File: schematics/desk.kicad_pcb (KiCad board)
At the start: 2 copper layers, 87 x 123 mm, 34 parts, among them K1 energized = UP (raises desk), K2 energized = DOWN (lowers desk), Q1 IRLZ44N, Q2 2N7000, Q3 2N7000, Q4 BC337, Q5 BC327, U1 LM2596HV 29V-5V, U2 ESP32_DevKitC, U3 74HC123 250ms, U5 ACS724xLCTR-05AB, U6 74HC08

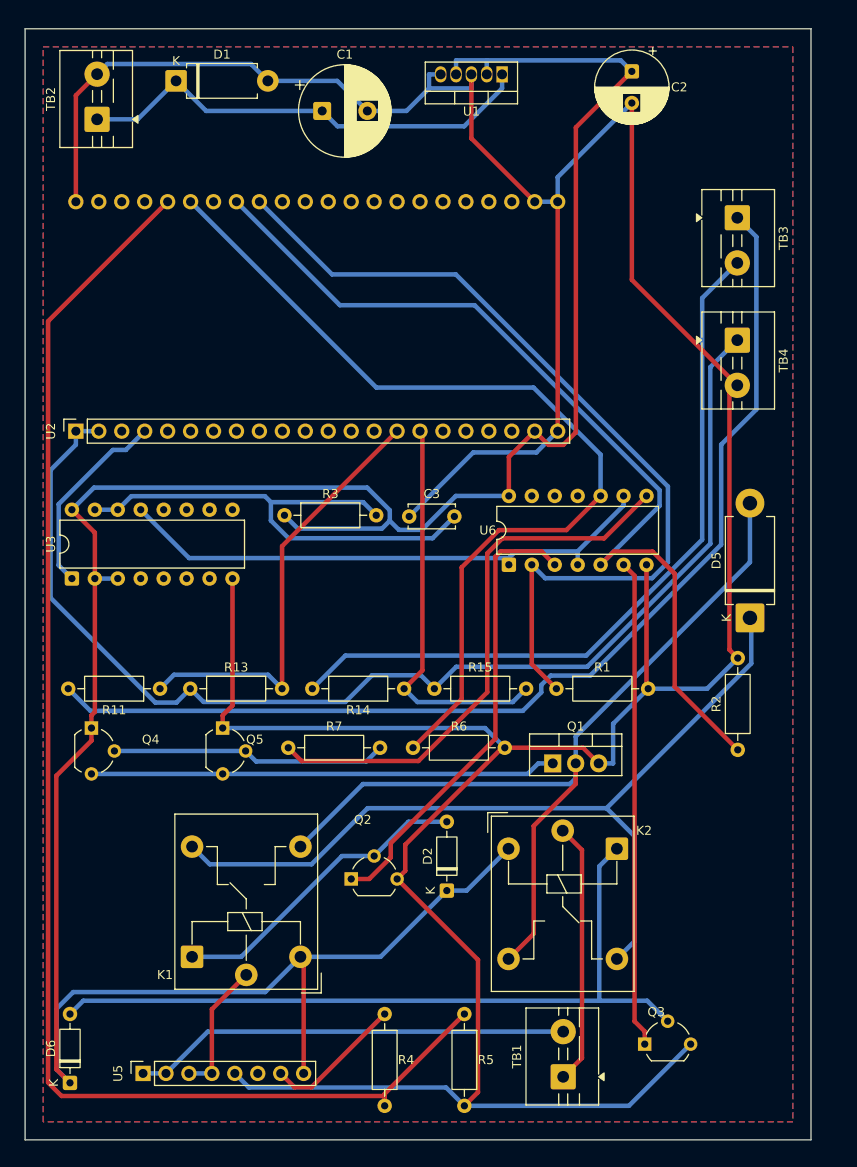
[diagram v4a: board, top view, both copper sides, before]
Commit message: Rotate R3/C3, shift U6/D5/R2/TB3/TB4 left: 87x123mm -> 85.5x123mm
R3 (12.3mm wide unrotated) and C3 (7.15mm wide unrotated) both have
much shorter dimensions on their other axis (6.44mm and 6.7mm) - both
fit easily within this row's height (driven by U6 at 18mm). Rotating
them 90 degrees freed 6.32mm of width in this row, which let U6, D5,
and R2 all shift left by that same amount.

R2 (now closer to R1 in the rocker row) needed a slightly smaller
shift than U6/D5 to keep 1.5mm clearance from R1 - not a uniform
block move, adjusted per-component to the nearest real constraint.

Once D5 stopped being the tightest thing in its row, TB3/TB4 (stacked
at the board's right edge) became the new binding width constraint
again - shifted them left too, down to what K2 (the actual widest
remaining item at 83.23mm) requires, rather than leaving them at the
old edge position out of inertia.

True footprint extent: 83.23 x 121.13mm (was 84.8 x 121.1mm - width
improved, height essentially unchanged since this pass didn't touch
row heights). Board outline: 85.5x123mm (was 87x123mm).

Re-routed from scratch, refilled both zones with the same settings as
recent commits. 0 vias, 0 unconnected, same accepted DRC profile
(isolated-copper + starved-thermal from the deliberate mill-fill
decision).
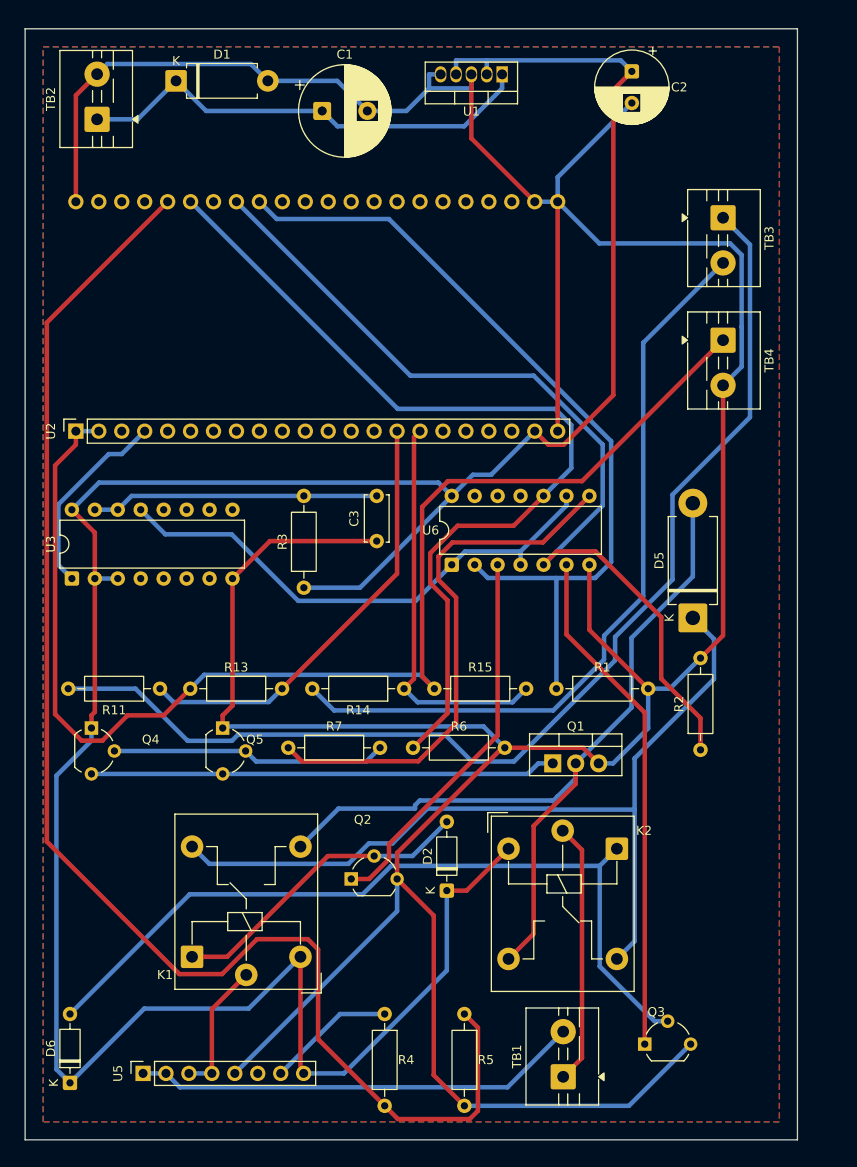
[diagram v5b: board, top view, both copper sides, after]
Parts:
- moved R3 8.30 mm to (30.9, 61.9), turned to 90 degrees
- moved D5 6.32 mm to (73.9, 65.2)
- moved U6 6.32 mm to (47.2, 59.3)
- moved C3 4.51 mm to (38.9, 56.7), turned to 90 degrees
- moved R2 4.12 mm to (74.8, 79.8)
- moved TB3 1.58 mm to (77.3, 20.9)
- moved TB4 1.58 mm to (77.3, 34.5)
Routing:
- net Net-(U3A-Cext): track 56.8 -> 31.8 mm
- net +3V3: track 133.5 -> 143.3 mm
- net Net-(Q2-G): track 50.9 -> 42.7 mm
- net DIR_A: track 97.9 -> 92.0 mm
- net Net-(TB3-Pin_1): track 120.1 -> 125.5 mm
- net +5V: track 294.6 -> 299.9 mm
- net Net-(D6-A): track 85.4 -> 89.3 mm
- net /WDOG: track 61.4 -> 58.2 mm
- net ISENSE: track 154.7 -> 157.6 mm
- net Net-(TB3-Pin_2): track 82.2 -> 85.0 mm
- net Net-(Q3-G): track 54.0 -> 56.7 mm
- net DIR_B: track 103.2 -> 100.8 mm
- net /MRET: track 96.8 -> 94.4 mm
- net PWM: track 102.4 -> 100.6 mm
- net Net-(R7-Pad1): track 61.4 -> 59.7 mm
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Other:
- board size 87 x 123 mm -> 85.5 x 123 mm

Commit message: Repack using courtyard-only bounds: 85.5x123mm -> 71x105mm
Silkscreen (reference/value text especially) doesn't matter for a
self-milled board - no printing step, and even the K1/K2 relay
footprints carry long descriptive Value strings ("energized = UP
(raises desk)") that were driving their bounding box far past the
real component body. K1 had drifted to x:-10mm (10mm off the board's
left edge) chasing exactly this - the real courtyard was only
4.3-20.6mm; the rest was that text field.

Re-derived every footprint's real (courtyard-only) size and rebuilt
placement from scratch on that basis, keeping the same functional
clusters and orientation choices already established this session
(TB3/TB4 stacked, R3/C3 rotated, D5/R2 relocated near the relays).
Sum of courtyard areas is 4202mm2 against the old board's 10516mm2 -
this pass gets to 7176mm2 (71x105mm), most of the remaining gap being
real routing/clearance overhead, not further squeeze-able footprint
bloat.

Packing this tight with plain shelf gaps left one net unrouted and
100 crossings for the router to fight through - not a routing rules
problem, just a placement the packer never optimized for routability
at all. Ran the KiCadRoutingTools quench optimizer (8mm displacement,
0.4mm clearance) with TB1-4 locked in place (edge connectors, no
reason to relocate them) before routing for real: crossings 153 -> 100,
28 other parts nudged, 0 overlaps introduced. Routed clean afterward:
0 unrouted, 4 vias.

DRC: 0 unconnected (real connectivity fully verified), plus a new
category of silk_overlap/silk_edge_clearance/silk_over_copper warnings
from packing components without regard for their labels - expected
and accepted per the reasoning above, same as the isolated-copper/
starved-thermal items already accepted in prior commits.
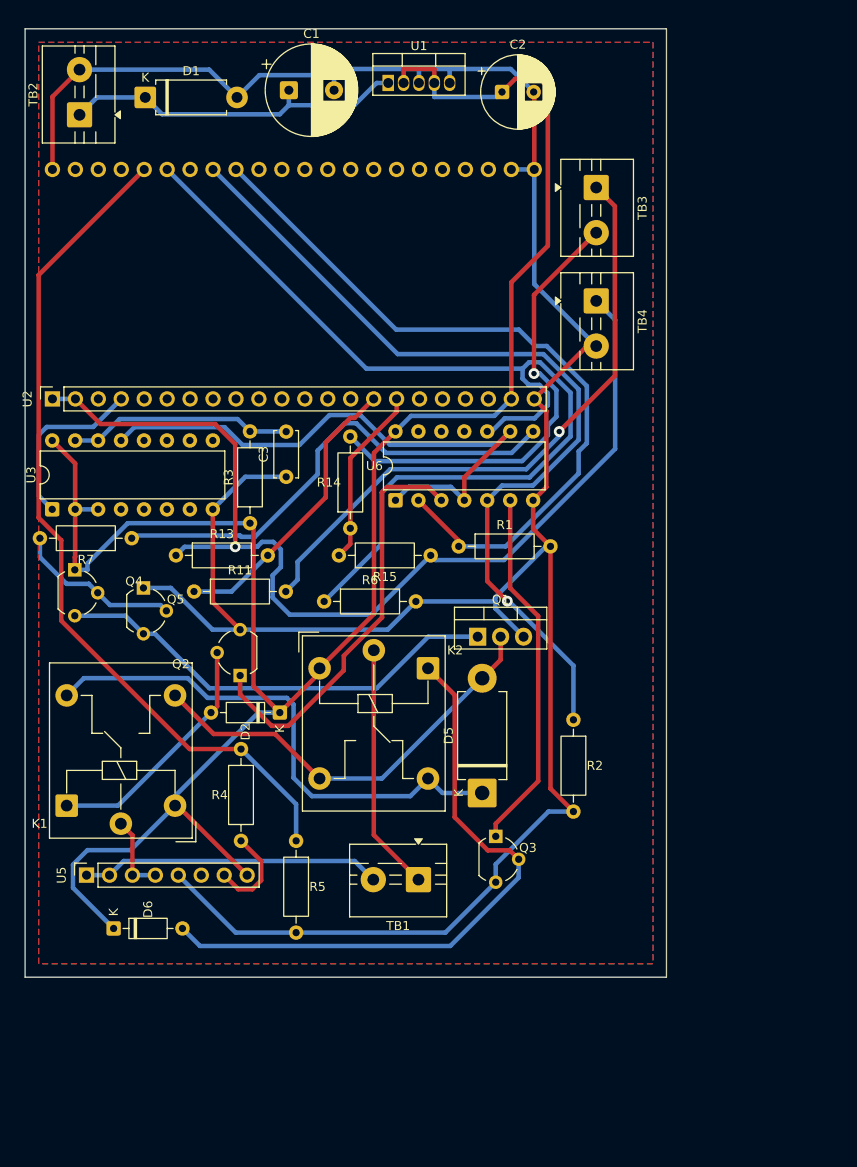
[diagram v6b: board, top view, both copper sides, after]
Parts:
- moved D5 30.3 mm to (50.6, 84.6)
- moved R7 29.0 mm to (11.8, 56.4), turned to 180 degrees
- moved K2 28.9 mm to (44.6, 70.8)
- moved Q3 28.3 mm to (52.1, 89.4), turned to -90 degrees
- moved TB1 27.1 mm to (43.5, 94.2), turned to 180 degrees
- moved D2 27.0 mm to (28.2, 75.7), turned to 180 degrees
- moved R5 26.7 mm to (30.0, 89.9)
- moved Q2 25.7 mm to (23.8, 71.6), turned to 90 degrees
- moved R4 24.9 mm to (23.9, 89.9), turned to 90 degrees
- moved U5 22.8 mm to (6.80, 93.7)
- moved K1 21.7 mm to (4.60, 86.0)
- moved R1 19.1 mm to (48.0, 57.3)
- moved R6 19.0 mm to (33.1, 63.4)
- moved R14 18.7 mm to (36.0, 55.3), turned to 90 degrees
- moved Q5 17.8 mm to (13.1, 61.9)
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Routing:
- net GND: track 411.0 -> 296.0 mm
- net +5V: track 299.9 -> 221.6 mm
- net ISENSE: track 157.6 -> 94.3 mm
- net Net-(TB3-Pin_1): track 125.5 -> 69.5 mm, vias 0 -> 1
- net /MRET: track 94.4 -> 47.9 mm
- net VSW: track 95.5 -> 58.4 mm
- net Net-(TB3-Pin_2): track 85.0 -> 51.3 mm, vias 0 -> 1
- net +3V3: track 143.3 -> 115.9 mm, vias 0 -> 1
- net SW_DN: track 44.0 -> 20.0 mm
- net Net-(D6-A): track 89.3 -> 69.9 mm
- net Net-(TB1-Pin_2): track 49.7 -> 33.3 mm
- net SW_UP: track 48.5 -> 32.3 mm
- net Net-(Q3-G): track 56.7 -> 40.4 mm
- net Net-(TB2-Pin_1): track 52.0 -> 38.8 mm
- net Net-(Q4-B): track 30.5 -> 18.6 mm
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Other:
- board size 85.5 x 123 mm -> 71 x 105 mm

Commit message: Shrink to 70x100mm - a standard pre-cut blank size
Confirmed this will be a pre-cut blank at exactly this size, not a
larger sheet trimmed down - so the generous 1.5-2mm edge margin used
throughout this session (protecting copper from an imprecise hand-
milled outline cut) doesn't apply here at all; there's no outline
pass. Dropped to 0.5mm, matching the board's own min_copper_edge_
clearance DRC rule instead of an arbitrary milling-safety number.

Even so, courtyard content needed 68.0 x 100.4mm at that margin - 0.4mm
over on height alone. Ran the quench optimizer again against a
pre-shrunk 70x100 outline (6mm displacement, TB1-4 still locked) to
find a fit; it got everything in except R5, left 1.09mm over the
bottom edge by itself. Moved R5 up by hand into the small gap between
the board edge budget and K2's own clearance requirement (both had to
be satisfied at once, window was under 0.1mm) - the only manual
placement change in this pass.

Recentered everything for even margins (1.41mm left/right, 0.81mm
top/bottom - the residual slack once the height constraint was
satisfied) rather than leaving it pinned to one corner.

Re-routed from scratch, refilled both zones at the new 0.5mm margin.
5 vias, 0 unconnected. Same accepted DRC profile as recent commits
(isolated-copper, starved-thermal, silk_* - all expected per the
courtyard-only placement and pre-cut-blank decisions already made
this session).
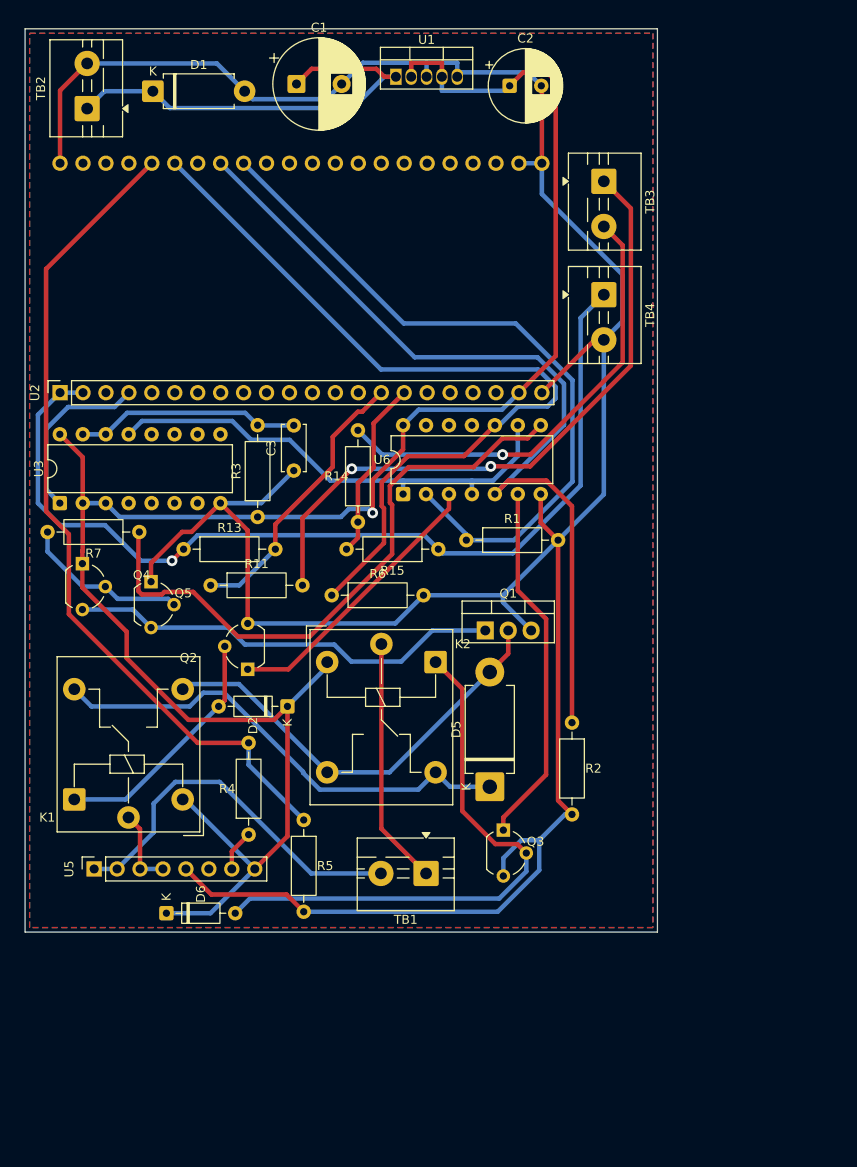
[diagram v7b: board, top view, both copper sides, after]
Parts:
- moved D6 6.08 mm to (15.6, 97.9)
- moved R5 2.46 mm to (30.8, 87.6)
- moved R11 1.97 mm to (20.5, 61.6)
- moved C1 1.09 mm to (30.0, 6.11)
- moved C2 1.09 mm to (53.6, 6.31)
- moved C3 1.09 mm to (29.7, 48.9)
- moved D2 1.09 mm to (29.0, 75.0)
- moved D5 1.09 mm to (51.4, 83.9)
- moved K2 1.09 mm to (45.4, 70.1)
- moved Q1 1.09 mm to (50.9, 66.6)
- moved Q3 1.09 mm to (52.9, 88.7)
- moved Q5 1.09 mm to (13.9, 61.2)
- moved R1 1.09 mm to (48.8, 56.6)
- moved R13 1.09 mm to (17.5, 57.6)
- moved R14 1.09 mm to (36.8, 54.6)
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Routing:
- net PWM: track 112.3 -> 91.8 mm
- net GND: track 296.0 -> 313.4 mm
- net Net-(Q2-G): track 46.4 -> 31.3 mm
- net Net-(R7-Pad1): track 53.7 -> 67.9 mm
- net /WDOG: track 66.4 -> 53.9 mm
- net Net-(TB2-Pin_1): track 38.8 -> 49.2 mm
- net +3V3: track 115.9 -> 105.8 mm
- net Net-(TB1-Pin_2): track 33.3 -> 41.8 mm
- net Net-(D6-A): track 69.9 -> 62.9 mm
- net +5V: track 221.6 -> 215.1 mm, vias 0 -> 1
- net Net-(U5-VIOUT): track 10.4 -> 4.57 mm
- net VSW: track 58.4 -> 53.4 mm
- net DIR_A: track 82.4 -> 79.0 mm
- net Net-(TB3-Pin_1): track 69.5 -> 72.4 mm, vias 1 -> 2
- net Net-(Q1-G): track 50.3 -> 48.4 mm
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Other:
- board size 71 x 105 mm -> 70 x 100 mm

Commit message: Add M3 mounting holes in all four corners
NPTH (unplated, no net) - purely mechanical, no reason to ground the
hardware here. Standard KiCad MountingHole_3.2mm_M3 footprint (3.2mm
drill, 3.45mm courtyard radius), 4mm inset from each edge - leaves
2.4mm of board material around the drill itself for structural
integrity, and clears the standard KiCad footprint's screw-head/washer
keepout from every nearby component.

Two of the four corners needed real changes to clear that keepout:

- Top-left (H1) directly overlapped TB2. The top row (TB2/D1/C1/U1/C2)
  had 10.3mm of unused width on its right end, so repacked the whole
  row into the window between both top corners' keepouts (7.5mm to
  62.4mm) with slightly tighter gaps (0.82mm) rather than restructuring
  anything - both TB2 and C2 now clear their respective corner hole
  with ~0.1mm to spare.
- Bottom-left (H3) was 1.25mm short of clearing U5. Shifted U5 right by
  1.9mm (moving it up first collided with K1 above; sideways had more
  room against R5).

Top-right and bottom-right didn't need any changes - already had
7.8mm+ of clearance from anything nearby.

Packing this tight left one net stuck unrouted again (same symptom as
the 70x100 pass) - ran the quench optimizer once more (4mm
displacement, TB1-4 and H1-4 all locked) before re-routing for real.
7 vias, 0 unconnected, same accepted DRC profile as recent commits.
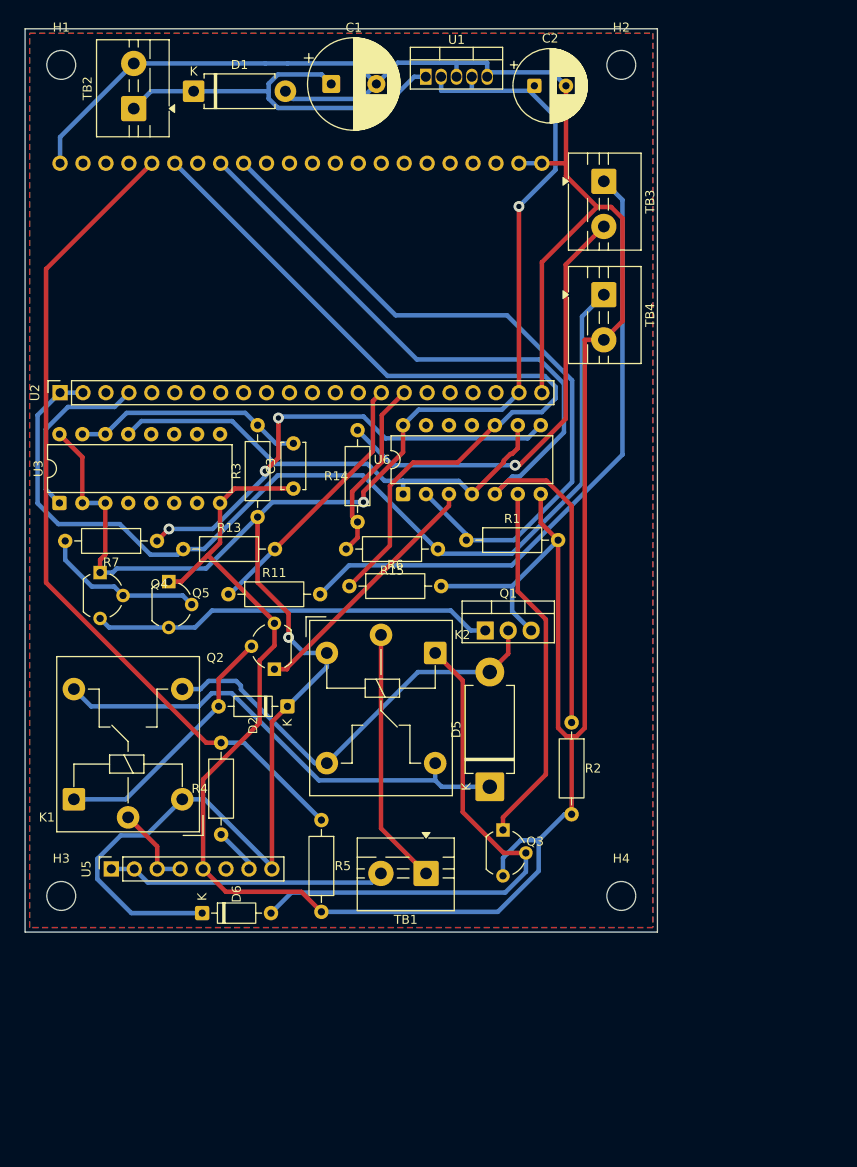
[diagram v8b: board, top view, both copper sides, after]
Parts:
- added H1: MountingHole_3.2mm_M3, MountingHole_3.2mm_M3, F.Cu at (4.00, 4.00)
- added H2: MountingHole_3.2mm_M3, MountingHole_3.2mm_M3, F.Cu at (66.0, 4.00)
- added H3: MountingHole_3.2mm_M3, MountingHole_3.2mm_M3, F.Cu at (4.00, 96.0)
- added H4: MountingHole_3.2mm_M3, MountingHole_3.2mm_M3, F.Cu at (66.0, 96.0)
- moved TB2 5.16 mm to (12.0, 8.84)
- moved D1 4.51 mm to (18.7, 6.91)
- moved D6 3.96 mm to (19.6, 97.9)
- moved C1 3.84 mm to (33.9, 6.11)
- moved U1 3.31 mm to (44.4, 5.31)
- moved R4 3.04 mm to (21.7, 89.2)
- moved Q2 2.96 mm to (27.6, 70.9)
- moved C2 2.73 mm to (56.4, 6.31)
- moved R6 2.20 mm to (35.9, 61.7)
- moved Q4 2.19 mm to (8.30, 60.2)
- moved R11 2.19 mm to (22.5, 62.6)
- moved R7 2.19 mm to (14.6, 56.7)
- moved C3 1.99 mm to (29.7, 50.9)
- moved Q5 1.96 mm to (15.9, 61.2)
- moved R5 1.96 mm to (32.8, 87.6)
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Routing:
- net GND: track 313.4 -> 362.6 mm
- net Net-(R7-Pad1): track 67.9 -> 52.7 mm, vias 0 -> 3
- net Net-(TB1-Pin_2): track 41.8 -> 30.9 mm
- net +3V3: track 105.8 -> 110.8 mm, vias 1 -> 0
- net Net-(TB2-Pin_1): track 49.2 -> 44.4 mm
- net Net-(Q1-G): track 48.4 -> 44.7 mm
- net Net-(Q2-G): track 31.3 -> 28.2 mm
- net Net-(D6-A): track 62.9 -> 59.9 mm
- net PWM: track 91.8 -> 89.0 mm
- net +5V: track 215.1 -> 213.1 mm, vias 1 -> 3
- net SW_UP: track 31.3 -> 29.4 mm
- net Net-(TB3-Pin_1): track 72.4 -> 71.0 mm, vias 2 -> 0
- net Net-(D2-A): track 27.2 -> 28.4 mm
- net Net-(TB1-Pin_1): track 27.4 -> 28.5 mm
- net /DRV_UP: track 8.77 -> 9.59 mm
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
